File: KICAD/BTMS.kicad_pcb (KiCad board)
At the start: 4 copper layers, 80.1 x 55.8 mm, 152 parts, among them J1 Batt_Ballance, J2 AUX_Charge, J3 Battery_IO, J4 Power_Out, J5 BT_LM62, J6 DSKY, J7 PWR_SW, J8 ICSP, J9 Heater, P1 USB_C_Plug, Q1 SSM3K341R, Q2 DMN65D8L, Q3 SSM3K341R, Q4 FDN340P, Q5 FDN340P, Q6 FDN340P, Q7 DMN65D8L, Q8 DMN65D8L, SW1 PTS526, U1 ACS711xLCTR-25AB, U10 BA033CC0FP-E2, U11 AON7522E, U12 AON7522E, U13 LM62CIM3/NOPB, U14 FAN3100TSX, U15 FAN3100TSX, U16 AON7522E, U17 dsPIC30F3011-PT, U18 FT230XQ, U2 AP33771, U3 IS281-4, U4 Q294700DSGR, U5 SCF4030-12-0X, U6 AONR21321, U7 ACS711xLCTR-25AB, U8 IS281-4, U9 IRS2184

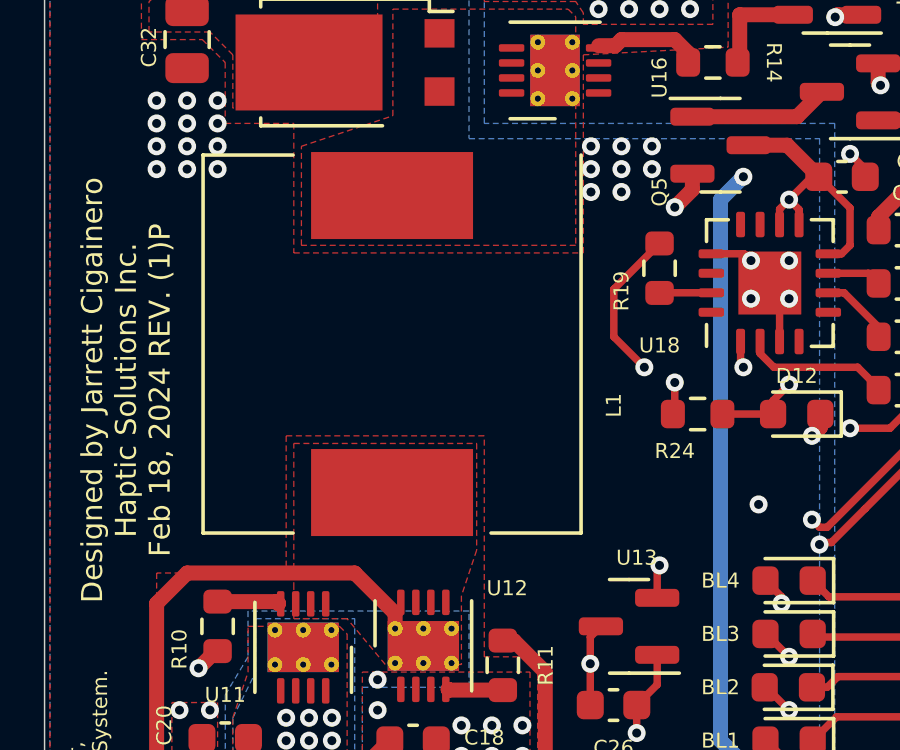
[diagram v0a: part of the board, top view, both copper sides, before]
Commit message: Cleaned up more tails and islands on PCB.
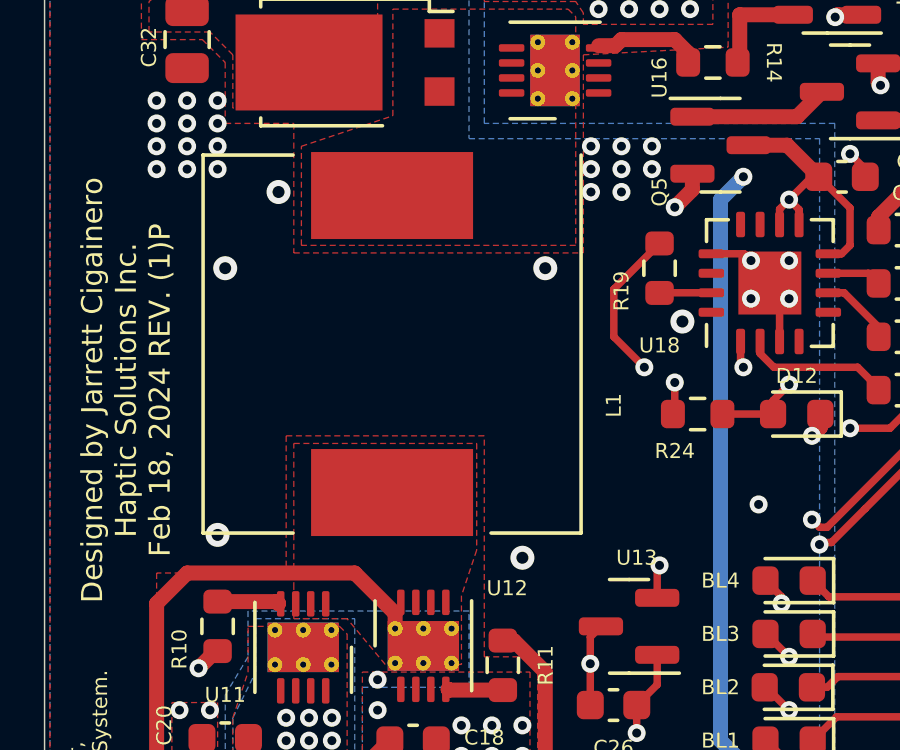
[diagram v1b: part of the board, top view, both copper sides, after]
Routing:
- net GND: vias 172 -> 178
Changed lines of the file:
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@@
   (via (at 167.386 105.918) (size 0.6) (drill 0.3) (layers "F.Cu" "B.Cu") (net 6))
   (via (at 155.481 134.399) (size 0.6) (drill 0.3) (layers "F.Cu" "B.Cu") (net 6))
+  (via (at 114.3 116.586) (size 0.8) (drill 0.4) (layers "F.Cu" "B.Cu") (free) (net 6))
   (via (at 112.522 132.588) (size 0.6) (drill 0.3) (layers "F.Cu" "B.Cu") (free) (net 6))
   (via (at 154.432 101.6) (size 0.6) (drill 0.3) (layers "F.Cu" "B.Cu") (net 6))
@@
   (via (at 132.08 97.028) (size 0.6) (drill 0.3) (layers "F.Cu" "B.Cu") (net 6))
   (via (at 142.57 136.22) (size 0.6) (drill 0.3) (layers "F.Cu" "B.Cu") (net 6))
+  (via (at 129.794 109.474) (size 0.8) (drill 0.4) (layers "F.Cu" "B.Cu") (free) (net 6))
   (via (at 168.402 104.902) (size 0.6) (drill 0.3) (layers "F.Cu" "B.Cu") (net 6))
   (via (at 178.562 115.57) (size 0.6) (drill 0.3) (layers "F.Cu" "B.Cu") (free) (net 6))
@@
   (via (at 165.608 126.492) (size 0.6) (drill 0.3) (layers "F.Cu" "B.Cu") (free) (net 6))
   (via (at 143.74 109.498) (size 0.6) (drill 0.3) (layers "F.Cu" "B.Cu") (net 6))
+  (via (at 125.222 107.696) (size 0.8) (drill 0.4) (layers "F.Cu" "B.Cu") (free) (net 6))
   (via (at 128.27 136.398) (size 0.6) (drill 0.3) (layers "F.Cu" "B.Cu") (net 6))
+  (via (at 114.554 107.696) (size 0.8) (drill 0.4) (layers "F.Cu" "B.Cu") (free) (net 6))
   (via (at 161.798 140.462) (size 0.5) (drill 0.25) (layers "F.Cu" "B.Cu") (free) (net 6))
   (via (at 159.766 140.462) (size 0.5) (drill 0.25) (layers "F.Cu" "B.Cu") (free) (net 6))
@@
   (via (at 114.3 102.108) (size 0.6) (drill 0.3) (layers "F.Cu" "B.Cu") (free) (net 6))
   (via (at 178.562 114.3) (size 0.6) (drill 0.3) (layers "F.Cu" "B.Cu") (free) (net 6))
+  (via (at 116.332 105.156) (size 0.8) (drill 0.4) (layers "F.Cu" "B.Cu") (free) (net 6))
+  (via (at 124.46 117.348) (size 0.8) (drill 0.4) (layers "F.Cu" "B.Cu") (free) (net 6))
   (via (at 145.288 138.43) (size 0.6) (drill 0.3) (layers "F.Cu" "B.Cu") (net 6))
   (via (at 169.418 102.87) (size 0.6) (drill 0.3) (layers "F.Cu" "B.Cu") (net 6))
@@
     (polygon
       (pts
+        (xy 121.412 135.636)
+        (xy 116.332 135.636)
+        (xy 116.332 132.842)
+        (xy 121.412 132.842)
+      )
+    )
+  )
+  (zone (net 0) (net_name "") (layer "In2.Cu") (hatch edge 0.508)
+    (connect_pads (clearance 0))
+    (min_thickness 0.254)
+    (keepout (tracks allowed) (vias allowed) (pads allowed) (copperpour not_allowed) (footprints allowed))
+    (fill (thermal_gap 0.508) (thermal_bridge_width 0.508))
+    (polygon
+      (pts
         (xy 185.928 101.092)
         (xy 186.944 102.87)
@@
     )
   )
+  (zone (net 0) (net_name "") (layer "B.Cu") (hatch edge 0.508)
+    (connect_pads (clearance 0))
+    (min_thickness 0.254)
+    (keepout (tracks allowed) (vias allowed) (pads allowed) (copperpour not_allowed) (footprints allowed))
+    (fill (thermal_gap 0.508) (thermal_bridge_width 0.508))
+    (polygon
+      (pts
+        (xy 119.126 133.604)
+        (xy 118.872 132.842)
+        (xy 120.396 132.842)
+      )
+    )
+  )
   (zone (net 6) (net_name "GND") (layer "B.Cu") (hatch edge 0.508)
     (connect_pads yes (clearance 0.2))
@@
   )
   (zone (net 0) (net_name "") (layer "B.Cu") (hatch edge 0.508)
+    (connect_pads (clearance 0))
+    (min_thickness 0.254)
+    (keepout (tracks allowed) (vias allowed) (pads allowed) (copperpour not_allowed) (footprints allowed))
+    (fill (thermal_gap 0.508) (thermal_bridge_width 0.508))
+    (polygon
+      (pts
+        (xy 180.34 99.568)
+        (xy 180.086 100.584)
+        (xy 177.546 99.314)
+      )
+    )
+  )
+  (zone (net 0) (net_name "") (layer "B.Cu") (hatch edge 0.508)
     (connect_pads yes (clearance 0))
     (min_thickness 0.254)
@@
     )
   )
+  (zone (net 0) (net_name "") (layer "B.Cu") (hatch edge 0.508)
+    (connect_pads (clearance 0))
+    (min_thickness 0.254)
+    (keepout (tracks allowed) (vias allowed) (pads allowed) (copperpour not_allowed) (footprints allowed))
+    (fill (thermal_gap 0.508) (thermal_bridge_width 0.508))
+    (polygon
+      (pts
+        (xy 177.8 127.254)
+        (xy 175.514 127.508)
+        (xy 175.514 126.746)
+      )
+    )
+  )
   (zone (net 12) (net_name "VBUS") (layer "B.Cu") (hatch edge 0.508)
     (connect_pads yes (clearance 0.2))
@@
       )
     )
+  )
+  (zone (net 0) (net_name "") (layer "B.Cu") (hatch edge 0.508)
+    (connect_pads (clearance 0))
+    (min_thickness 0.254)
+    (keepout (tracks allowed) (vias allowed) (pads allowed) (copperpour not_allowed) (footprints allowed))
+    (fill (thermal_gap 0.508) (thermal_bridge_width 0.508))
+    (polygon
+      (pts
+        (xy 181.864 101.6)
+        (xy 182.88 102.108)
+        (xy 182.88 102.616)
+        (xy 179.07 102.616)
+        (xy 174.244 102.87)
+        (xy 174.498 101.346)
+      )
+    )

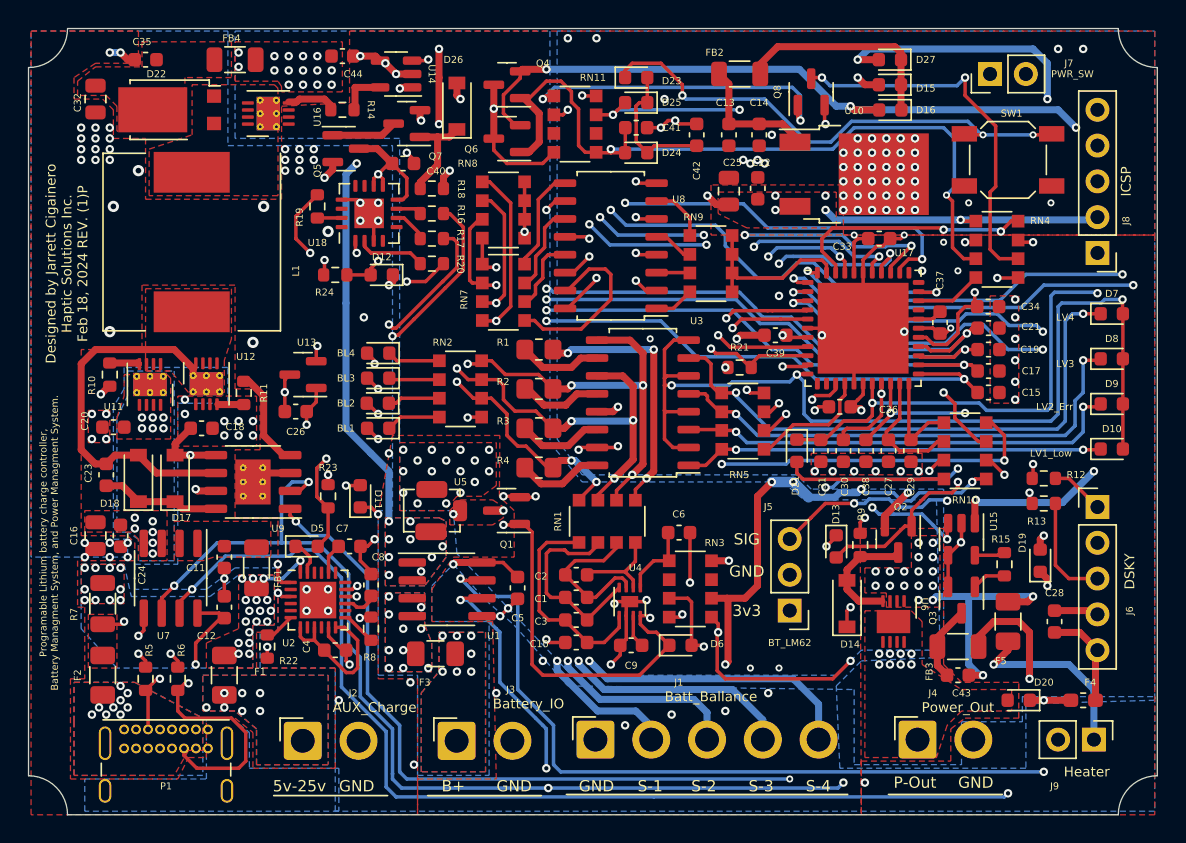
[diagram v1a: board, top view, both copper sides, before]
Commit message: Cleaned up more tails and islands on PCB.
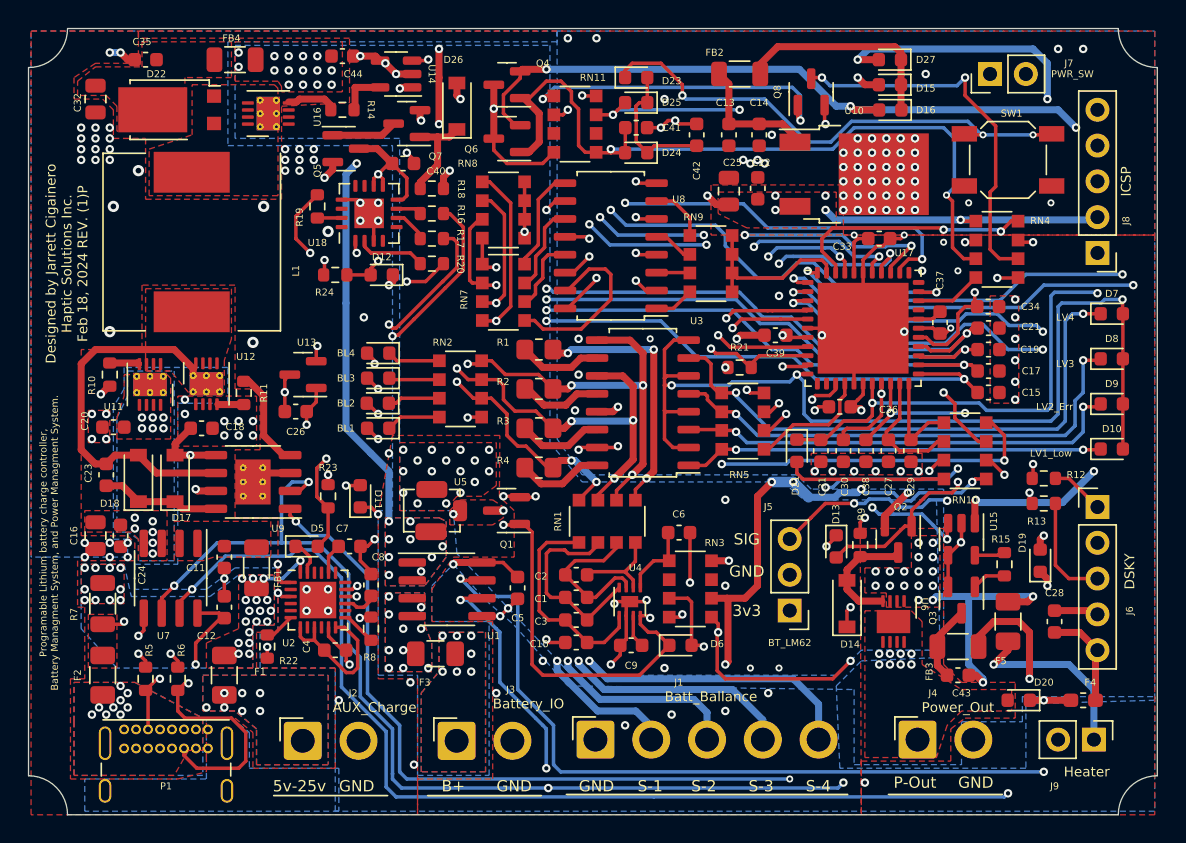
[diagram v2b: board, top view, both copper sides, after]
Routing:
- net /ExtBus: track 19.1 -> 19.6 mm
- net GND: vias 178 -> 185

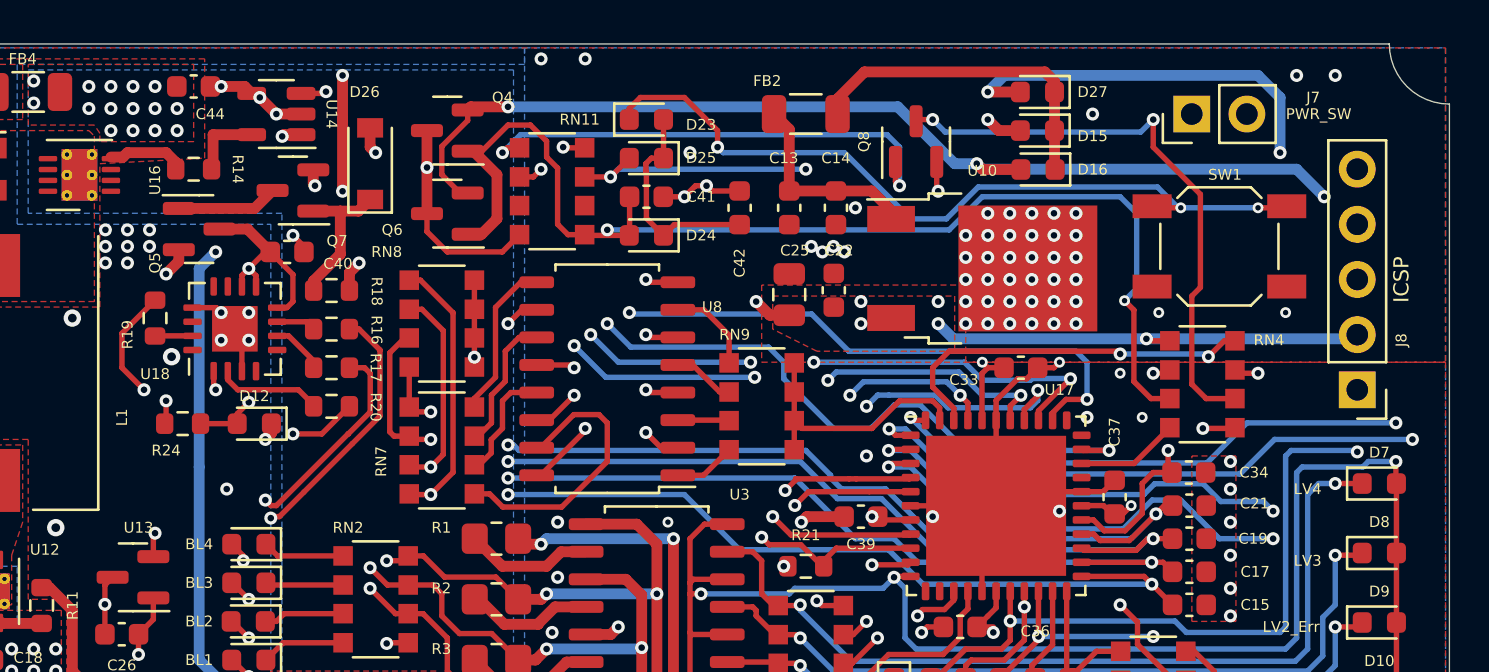
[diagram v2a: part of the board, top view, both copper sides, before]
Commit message: Added 10K pullup resistors to dsPIC's serial RX lines.
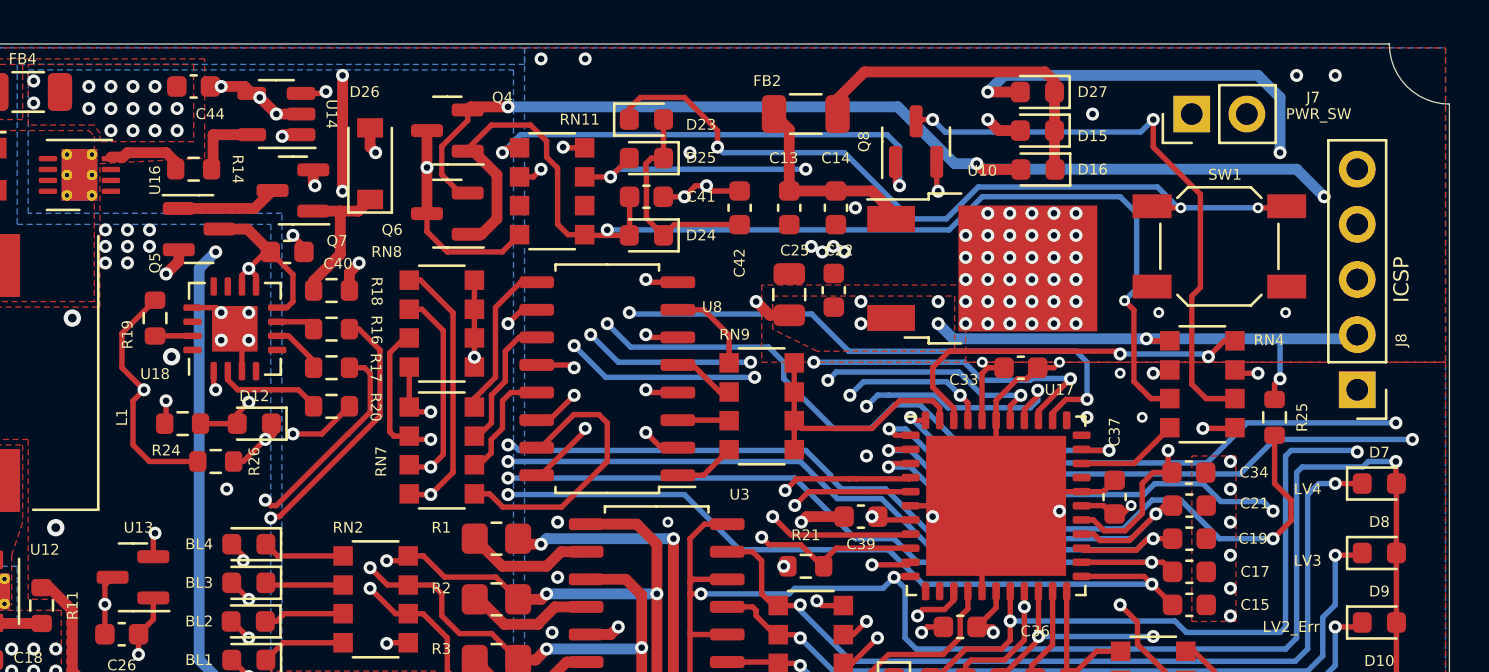
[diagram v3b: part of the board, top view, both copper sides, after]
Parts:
- added R25: 10K, Resistor_SMD:R_0603_1608Metric, F.Cu at (180.6, 112.3)
- added R26: 10K, Resistor_SMD:R_0603_1608Metric, F.Cu at (131.8, 114.3)
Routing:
- net /U1RX: track 58.2 -> 64.3 mm
- net /U2RX: track 30.7 -> 36.1 mm
- net +5C: track 215.3 -> 220.1 mm, vias 22 -> 23

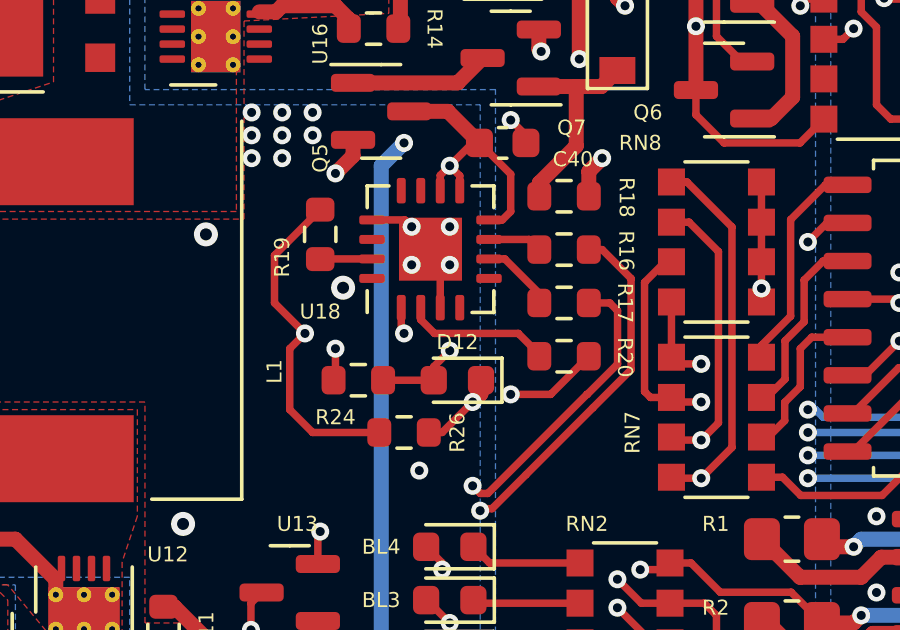
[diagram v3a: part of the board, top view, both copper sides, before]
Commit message: Added ground connection to CTS pin on FTDI chip.
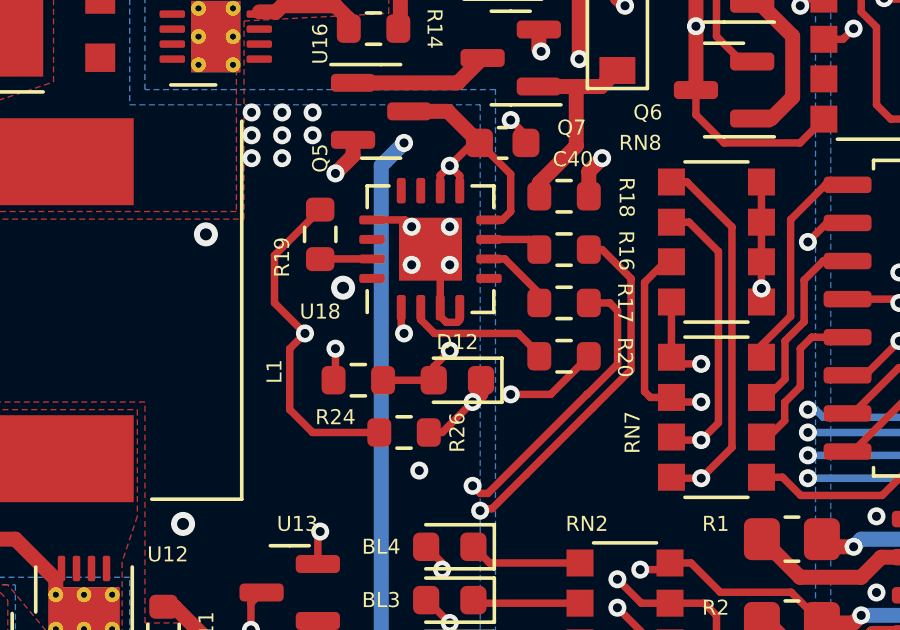
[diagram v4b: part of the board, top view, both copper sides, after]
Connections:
- U18 pad 4: unconnected-(U18-Pad4) -> GND
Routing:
- net GND: track 110.8 -> 112.2 mm
